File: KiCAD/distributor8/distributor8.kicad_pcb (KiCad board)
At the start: 4 copper layers, 431.8 x 25.4 mm, 29 parts, among them P1 CONN_02X03, P11 CONN_02X03, P13 CONN_02X03, P15 CONN_02X03, P17 CONN_02X03, P19 CONN_02X03, P23 CONN_02X07, P24 CONN_02X07, P29 CONN_02X07, P3 CONN_02X03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

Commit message: switch to step for 3d
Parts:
- P1, P11, P13, P15, P17, P19, P3, P31, P32, P39, P40, P47, P48, P5, P7, P9: footprint myParts:TMS-103-02-L-D-SE -> myParts:TMS-103-01-L-D-SE

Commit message: change d8 header
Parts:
- removed P47: CONN_02X03, myParts:TMS-103-01-L-D-SE
- P23, P24, P29, P30, P37, P38, P45, P46: footprint Pin_Headers:Pin_Header_Angled_2x07_Pitch2.54mm -> myParts:SSW-107-02-T-D-RA; moved to B.Cu
- turned P23 to 90 degrees
- turned P24 to 90 degrees
- turned P29 to 90 degrees
- turned P30 to 90 degrees
- turned P37 to 90 degrees
- turned P38 to 90 degrees
- turned P45 to 90 degrees
- turned P46 to 90 degrees

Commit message: fix board assembly
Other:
- board text added: "7adbde5"
- board text removed: "v0.11"
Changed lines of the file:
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@@
   (gr_line (start 0 10) (end 0 0) (angle 90) (layer F.SilkS) (width 0.2))
   (gr_line (start 30 10) (end 30 0) (angle 90) (layer F.SilkS) (width 0.2))
-  (gr_text v0.11 (at 405.79 5.69) (layer F.SilkS)
+  (gr_text 7adbde5 (at 405.79 5.69) (layer F.SilkS)
     (effects (font (size 1.5 1.5) (thickness 0.3)))
   )

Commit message: try to fix messed up d8 routing
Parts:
- added P47: CONN_02X03, myParts:TMS-103-01-L-D-SE, F.Cu at (250.6, 1.90)
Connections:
- P29 pad 1: H0_V -> F0_V
- P29 pad 10: H4_I -> F4_I
- P29 pad 11: HR_V -> FR_V
- P29 pad 12: HR_I -> FR_I
- P29 pad 2: H0_I -> F0_I
- P29 pad 3: D2_V -> F2_V
- P29 pad 4: H2_I -> F2_I
- P29 pad 9: H4_V -> F4_V
- P31 pad 1: H0_V -> F0_V
- P31 pad 2: H0_I -> F0_I
- P31 pad 3: D2_V -> F2_V
- P31 pad 4: H2_I -> F2_I
- P32 pad 3: H4_V -> F4_V
- P32 pad 4: H4_I -> F4_I
- P32 pad 5: HR_V -> FR_V
- P32 pad 6: HR_I -> FR_I
- P38 pad 1: F0_V -> G0_V
- P38 pad 10: F4_I -> G4_I
- P38 pad 11: FR_V -> GR_V
- P38 pad 12: FR_I -> GR_I
- P38 pad 2: F0_I -> G0_I
- P38 pad 3: F2_V -> G2_V
- P38 pad 4: F2_I -> G2_I
- P38 pad 9: F4_V -> G4_V
- P39 pad 1: F0_V -> SCL
- P39 pad 2: F0_I -> SDA
- P39 pad 3: F2_V -> G4_V
- P39 pad 4: F2_I -> G4_I
- P39 pad 5: MISO -> GR_V
- P39 pad 6: MOSI -> GR_I
- P40 pad 1: SCL -> G0_V
- P40 pad 2: SDA -> G0_I
- P40 pad 3: F4_V -> G2_V
- P40 pad 4: F4_I -> G2_I
- P40 pad 5: FR_V -> MISO
- P40 pad 6: FR_I -> MOSI
- P46 pad 1: G0_V -> H0_V
- P46 pad 10: G4_I -> H4_I
- P46 pad 11: GR_V -> HR_V
- P46 pad 12: GR_I -> HR_I
- P46 pad 2: G0_I -> H0_I
- P46 pad 3: G2_V -> D2_V
- P46 pad 4: G2_I -> H2_I
- P46 pad 9: G4_V -> H4_V
- P48 pad 1: SCL -> H0_V
- P48 pad 2: SDA -> H0_I
- P48 pad 3: G4_V -> D2_V
- P48 pad 4: G4_I -> H2_I
- P48 pad 5: GR_V -> MISO
- P48 pad 6: GR_I -> MOSI
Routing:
- net MISO: track 466.0 -> 0.00 mm, vias 11 -> 0
- net MOSI: track 459.1 -> 0.00 mm, vias 11 -> 0
- net SCL: track 434.1 -> 0.00 mm, vias 10 -> 0
- net SDA: track 426.8 -> 0.00 mm, vias 9 -> 0
- net A0_V: track 319.5 -> 0.00 mm, vias 3 -> 0
- net C0_V: track 305.8 -> 0.00 mm, vias 5 -> 0
- net A2_I: track 298.0 -> 0.00 mm, vias 3 -> 0
- net B0_I: track 295.1 -> 0.00 mm, vias 2 -> 0
- net A0_I: track 293.7 -> 0.00 mm, vias 1 -> 0
- net B0_V: track 293.6 -> 0.00 mm, vias 5 -> 0
- net A2_V: track 285.1 -> 0.00 mm, vias 1 -> 0
- net D2_V: track 280.4 -> 0.00 mm, vias 2 -> 0
- net B2_I: track 279.8 -> 0.00 mm, vias 1 -> 0
- net C2_I: track 277.2 -> 0.00 mm, vias 2 -> 0
- net C0_I: track 273.0 -> 0.00 mm, vias 1 -> 0
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
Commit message: fixed d8
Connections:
- P46 pad 3: D2_V -> H2_V
- P48 pad 3: D2_V -> H2_V
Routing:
- net SDA: track 0.00 -> 529.9 mm, vias 0 -> 10
- net MOSI: track 0.00 -> 468.1 mm, vias 0 -> 14
- net MISO: track 0.00 -> 427.2 mm, vias 0 -> 11
- net SCL: track 0.00 -> 401.4 mm, vias 0 -> 9
- net E2_V: track 0.00 -> 359.6 mm, vias 0 -> 7
- net E4_V: track 0.00 -> 355.7 mm, vias 0 -> 4
- net A0_I: track 0.00 -> 300.7 mm, vias 0 -> 1
- net FR_V: track 0.00 -> 297.8 mm, vias 0 -> 4
- net A2_I: track 0.00 -> 289.1 mm, vias 0 -> 2
- net A0_V: track 0.00 -> 286.0 mm, vias 0 -> 1
- net B0_I: track 0.00 -> 285.0 mm, vias 0 -> 1
- net A2_V: track 0.00 -> 280.9 mm
- net B2_I: track 0.00 -> 279.7 mm, vias 0 -> 1
- net B0_V: track 0.00 -> 278.4 mm, vias 0 -> 4
- net C2_I: track 0.00 -> 271.1 mm, vias 0 -> 2
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
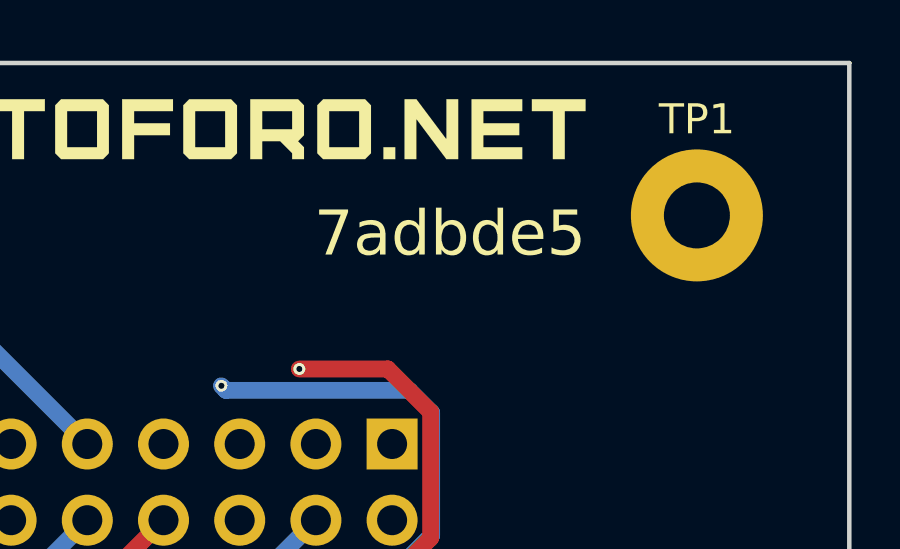
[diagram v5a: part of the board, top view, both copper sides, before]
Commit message: updage silkscreen hash and gen manufacturing files
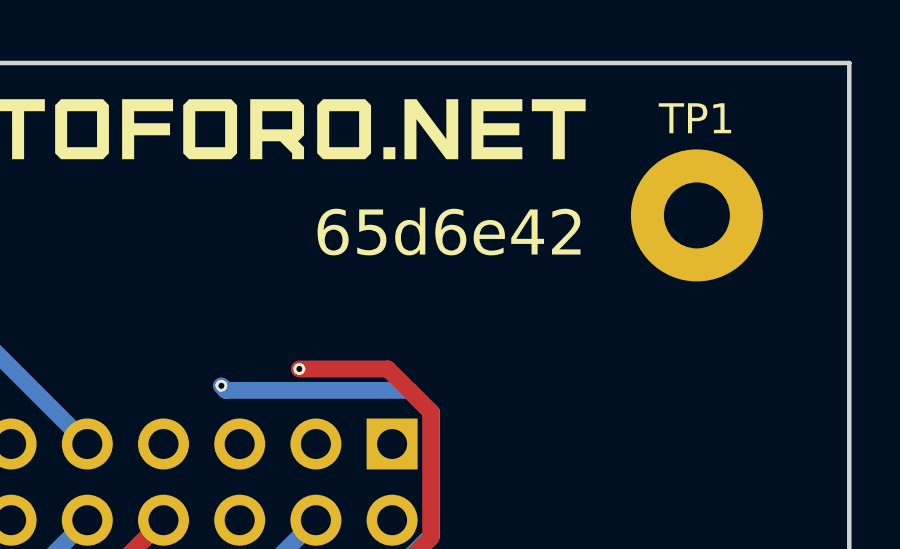
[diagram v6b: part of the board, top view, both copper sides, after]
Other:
- board text added: "65d6e42"
- board text removed: "7adbde5"
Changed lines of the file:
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@@
   (gr_line (start 0 10) (end 0 0) (angle 90) (layer F.SilkS) (width 0.2))
   (gr_line (start 30 10) (end 30 0) (angle 90) (layer F.SilkS) (width 0.2))
-  (gr_text 7adbde5 (at 405.79 5.69) (layer F.SilkS)
+  (gr_text 65d6e42 (at 405.79 5.69) (layer F.SilkS)
     (effects (font (size 1.5 1.5) (thickness 0.3)))
   )

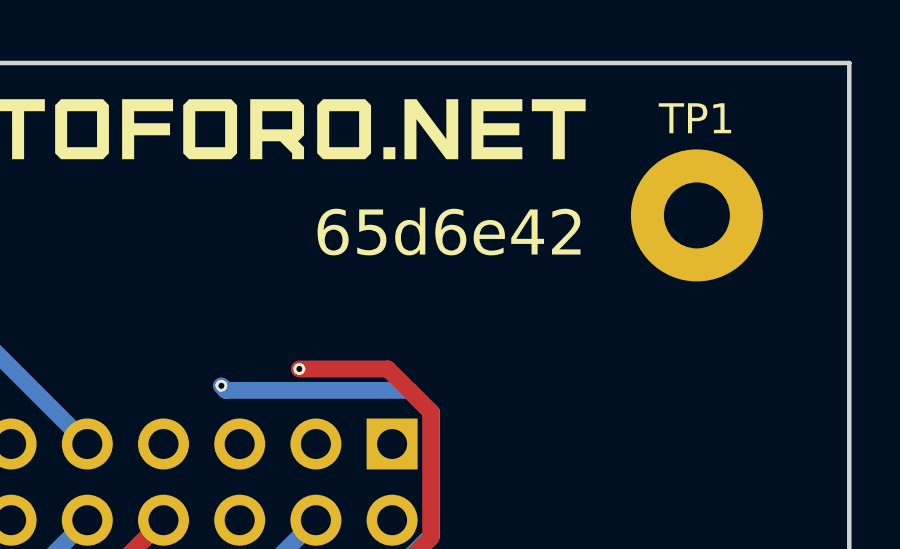
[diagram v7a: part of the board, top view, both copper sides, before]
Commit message: generate order packages
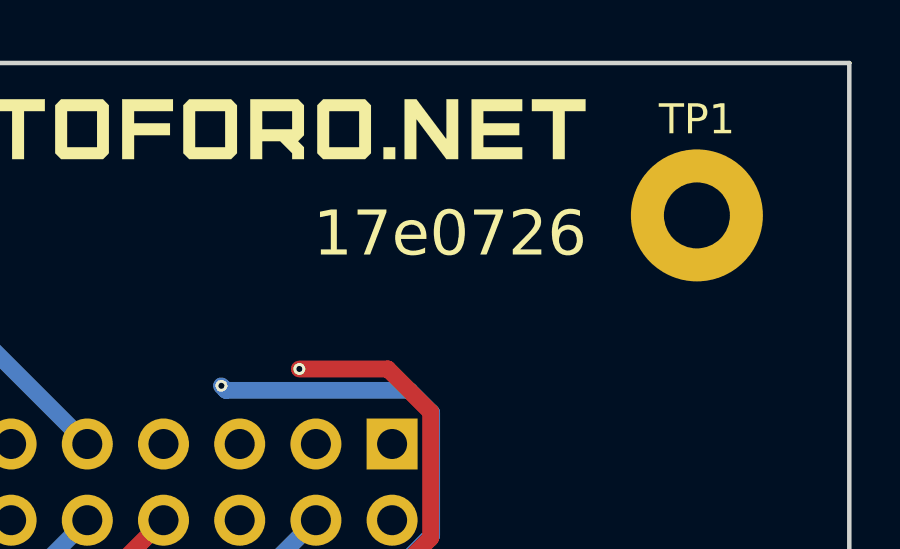
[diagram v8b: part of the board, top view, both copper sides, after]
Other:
- board text added: "17e0726"
- board text removed: "65d6e42"
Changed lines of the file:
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@@
   (gr_line (start 0 10) (end 0 0) (angle 90) (layer F.SilkS) (width 0.2))
   (gr_line (start 30 10) (end 30 0) (angle 90) (layer F.SilkS) (width 0.2))
-  (gr_text 65d6e42 (at 405.79 5.69) (layer F.SilkS)
+  (gr_text 17e0726 (at 405.79 5.69) (layer F.SilkS)
     (effects (font (size 1.5 1.5) (thickness 0.3)))
   )
